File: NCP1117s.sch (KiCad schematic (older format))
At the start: 15 parts, among them U17 NCP1117ST18T3G, U18 NCP1117ST33T3G, U19 NCP1117ST50T3G

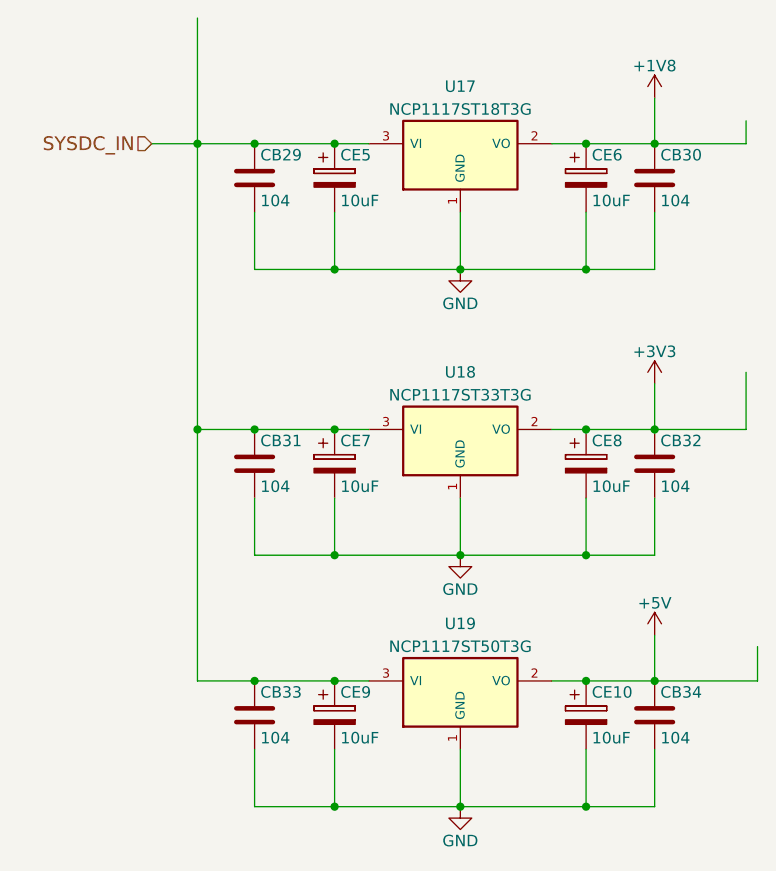
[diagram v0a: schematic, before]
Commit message: Deleted unnecessary files and splitting schmatics.
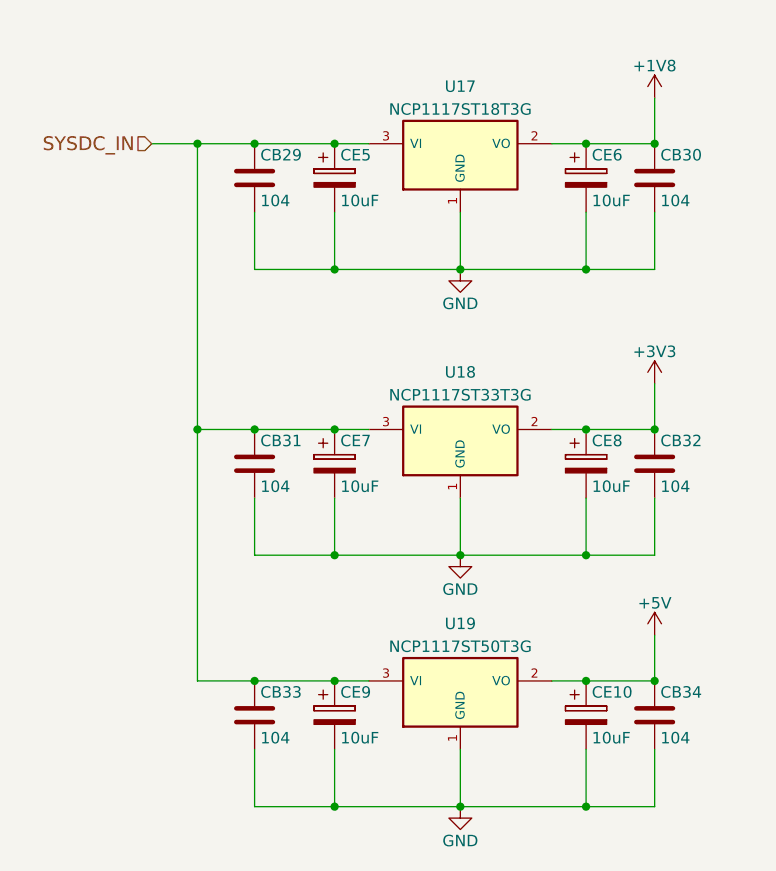
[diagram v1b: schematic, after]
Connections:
- wire segments 31 -> 28
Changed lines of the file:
@@
 $Descr A4 11693 8268
 encoding utf-8
-Sheet 7 7
-Title ""
+Sheet 8 8
+Title "DCoJA Yatagarasu Mezzanine"
 Date ""
 Rev ""
-Comp ""
-Comment1 ""
-Comment2 ""
-Comment3 ""
-Comment4 ""
+Comp "DroneWorks Inc."
+Comment1 "Copyright (c) 2016 DroneWorks Inc."
+Comment2 "All rights reserved."
+Comment3 "Creative Commons  (CC BY-SA 4.0)"
+Comment4 "Designed by: Michihiro Imaoka (@imaoca)"
+Comment5 "LDO"
 $EndDescr
 $Comp
-L GND #PWR0101
+L GND #PWR099
 U 1 1 5707ADD4
 P 5300 3000
-F 0 "#PWR0101" H 5300 2750 50  0001 C CNN
+F 0 "#PWR099" H 5300 2750 50  0001 C CNN
 F 1 "GND" H 5300 2850 50  0000 C CNN
 F 2 "" H 5300 3000 60  0000 C CNN
@@
 	3950 2450 4900 2450
 Wire Wire Line
-	5700 2450 6550 2450
-Wire Wire Line
 	4400 2750 4400 3000
 Wire Wire Line
@@
 Connection ~ 5850 3000
 $Comp
-L GND #PWR0102
+L GND #PWR0100
 U 1 1 5707AE00
 P 5300 4250
-F 0 "#PWR0102" H 5300 4000 50  0001 C CNN
+F 0 "#PWR0100" H 5300 4000 50  0001 C CNN
 F 1 "GND" H 5300 4100 50  0000 C CNN
 F 2 "" H 5300 4250 60  0000 C CNN
@@
 	4150 3700 4900 3700
 Wire Wire Line
-	5700 3700 6550 3700
+	5700 3700 6150 3700
 Wire Wire Line
 	4400 4000 4400 4250
@@
 Connection ~ 5850 4250
 $Comp
-L GND #PWR0103
+L GND #PWR0101
 U 1 1 5707AE2C
 P 5300 5350
-F 0 "#PWR0103" H 5300 5100 50  0001 C CNN
+F 0 "#PWR0101" H 5300 5100 50  0001 C CNN
 F 1 "GND" H 5300 5200 50  0000 C CNN
 F 2 "" H 5300 5350 60  0000 C CNN
@@
 	4150 4800 4900 4800
 Wire Wire Line
-	5700 4800 6600 4800
-Wire Wire Line
 	4400 5100 4400 5350
 Wire Wire Line
@@
 Text HLabel 3950 2450 0    60   Input ~ 0
 SYSDC_IN
-Wire Wire Line
-	4150 1900 4150 4800
 Connection ~ 4150 3700
 Connection ~ 4150 2450
@@
 Connection ~ 4400 3700
 Connection ~ 4400 4800
-Wire Wire Line
-	6600 4800 6600 4650
 Connection ~ 6150 4800
-Wire Wire Line
-	6550 3700 6550 3450
 Connection ~ 6150 3700
-Wire Wire Line
-	6550 2450 6550 2350
 Connection ~ 6150 2450
 $Comp
-L +5V #PWR0104
+L +5V #PWR0102
 U 1 1 573C0E74
 P 6150 4600
-F 0 "#PWR0104" H 6150 4450 50  0001 C CNN
+F 0 "#PWR0102" H 6150 4450 50  0001 C CNN
 F 1 "+5V" H 6150 4740 50  0000 C CNN
 F 2 "" H 6150 4600 50  0000 C CNN
@@
 $EndComp
 $Comp
-L +1V8 #PWR0105
+L +1V8 #PWR0103
 U 1 1 573FCFB3
 P 6150 2250
-F 0 "#PWR0105" H 6150 2100 50  0001 C CNN
+F 0 "#PWR0103" H 6150 2100 50  0001 C CNN
 F 1 "+1V8" H 6150 2390 50  0000 C CNN
 F 2 "" H 6150 2250 50  0000 C CNN
@@
 $EndComp
 $Comp
-L +3V3 #PWR0106
+L +3V3 #PWR0104
 U 1 1 573FD026
 P 6150 3500
-F 0 "#PWR0106" H 6150 3350 50  0001 C CNN
+F 0 "#PWR0104" H 6150 3350 50  0001 C CNN
 F 1 "+3V3" H 6150 3640 50  0000 C CNN
 F 2 "" H 6150 3500 50  0000 C CNN
@@
 	1    0    0    -1
 $EndComp
+Wire Wire Line
+	5700 2450 6150 2450
+Wire Wire Line
+	5700 4800 6150 4800
+Wire Wire Line
+	4150 2450 4150 4800
 $EndSCHEMATC
